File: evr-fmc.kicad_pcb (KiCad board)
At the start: 6 copper layers, 84 x 69 mm, 255 parts, among them J1 MMCX, J10 MMCX, J11 MMCX, J12 MMCX, J13 MMCX, J14 MMCX, J15 MMCX, J16 MMCX, J19 WP Jumper, J2 MMCX, J3 MMCX, J4 MMCX, J5 MMCX, J6 MMCX, J7 MMCX, J8 MMCX, J9 MMCX, P1 ASP-134488-01, Q1 FDN335N, Q2 FDN335N, Q3 FDN335N, T1 TCM2-43X+, T2 TCM2-43X+, T3 TCM2-43X+, T4 TCM2-43X+, U1 SN74LVC3G34DCT, U10 SN74LVC3G34DCT, U11 SN74LVC3G34DCT, U12 SN74LVC3G34DCT, U13 SN74LVC3G34DCT, U14 SN74LVC3G34DCT, U15 SN74LVC3G34DCT, U16 SN74LVC3G34DCT, U17 SN74LVC3G34DCT, U18 SI5394, U19 SI5394, U2 SN74LVC3G34DCT, U20 TLV75733PDBV, U21 TLV75718PDBV, U22 TPS562200, U23 74AVC4T245, U24 TLV75733PDBV, U25 74AVC4T245, U26 74LVC8T245, U27 74LVC8T245, U28 TLV75718PDBV, U3 SN74LVC3G34DCT, U4 SN74LVC3G34DCT, U5 SN74LVC3G34DCT, U6 SN74LVC3G34DCT, U7 SN74LVC3G34DCT, U8 SN74LVC3G34DCT, U9 AT24C64D, Y1 CX3225SB48000D0FPJC1, Y2 CX3225SB48000D0FPJC1

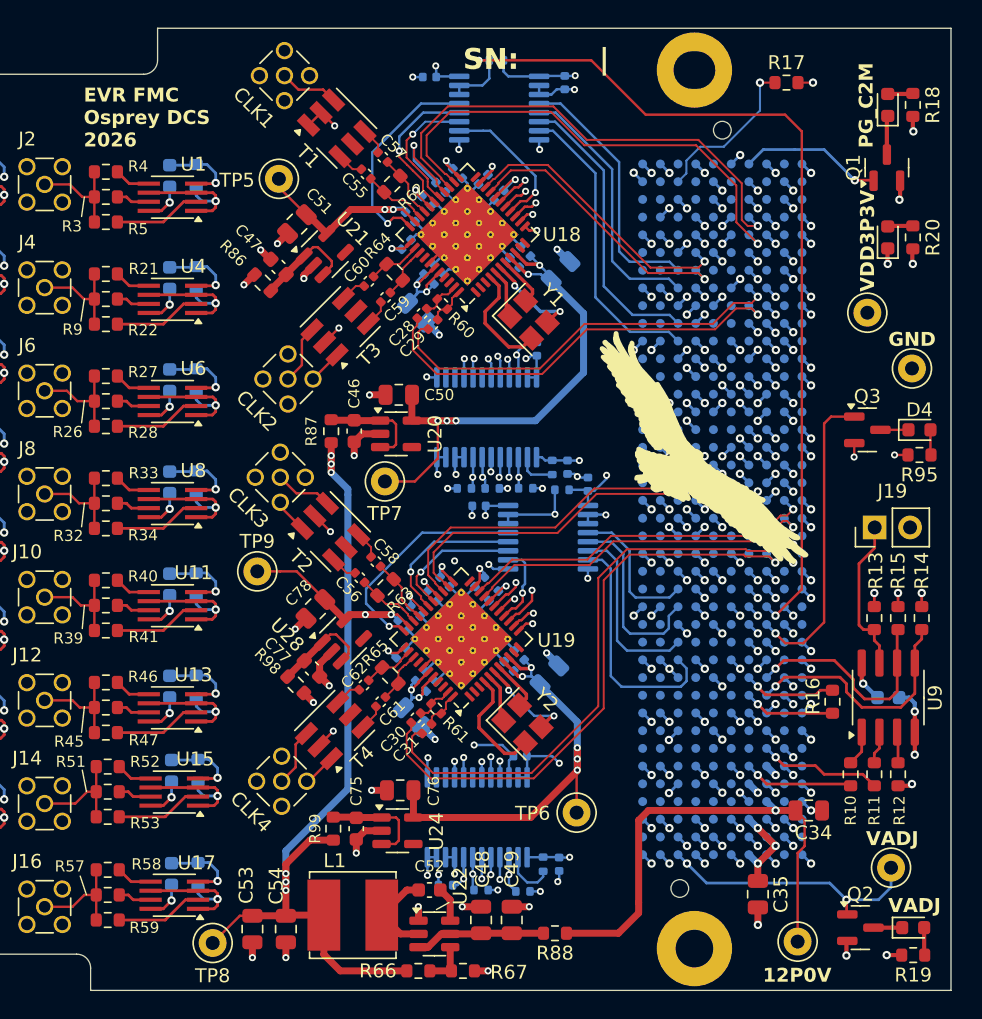
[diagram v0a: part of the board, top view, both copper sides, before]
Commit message: Final Draft - Ready for review
Updates:
- Changed area behind FMC connector to match the new Osprey FMC template
  - This includes a new 12V LED, more robust power input traces, arranged elements for readability.

Things to do:
Round diff traces before generating fabrication files
Change name of project to 'trigger output fmc'
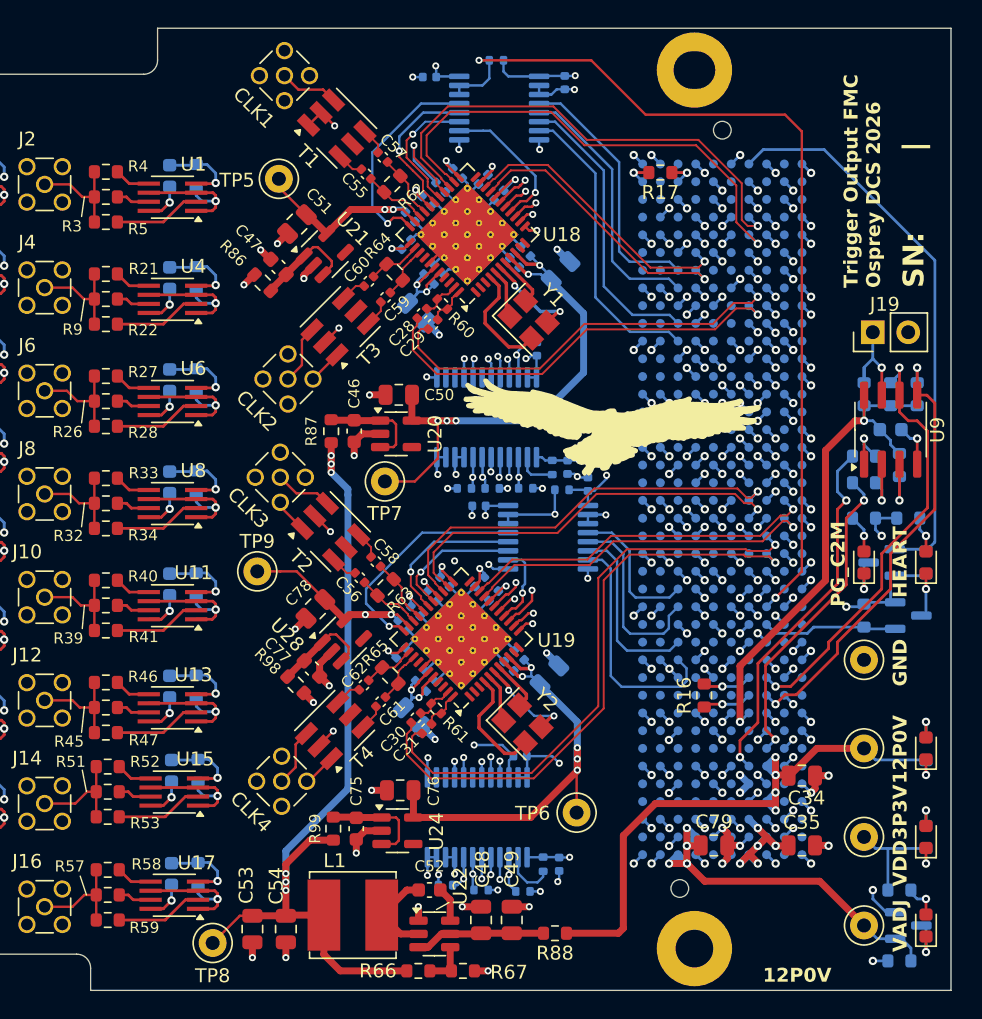
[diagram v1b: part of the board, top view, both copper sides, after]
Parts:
- added C79: 22uF, Capacitor_SMD:C_0805_2012Metric, F.Cu at (174.0, 129.6)
- added D5: Green, LED_SMD:LED_0603_1608Metric, F.Cu at (189.2, 122.6)
- added R100: 8.2k, Resistor_SMD:R_0603_1608Metric, B.Cu at (189.2, 122.7)
- added R101: 100k, Resistor_SMD:R_0603_1608Metric, B.Cu at (189.2, 109.3)
- added R102: 100k, Resistor_SMD:R_0603_1608Metric, B.Cu at (187.3, 137.9)
- added R103: 100k, Resistor_SMD:R_0603_1608Metric, B.Cu at (184.8, 113.1)
- D1, D2, D3, D4: value LED_Green -> Green
- Q1, Q2, Q3, R10, R11, R12, R13, R14, R15, R18, R19, R20, R95: moved to B.Cu
- TP5, TP9: value 1P8V -> Keystone5000
- TP6, TP7: value 3P3V -> Keystone5000
- TP8: value 4P3V -> Keystone5000
- moved D3 43.1 mm to (189.2, 129.0)
- moved R20 43.0 mm to (189.2, 129.0)
- moved TP3 37.6 mm to (184.8, 129.0)
- moved D1 32.9 mm to (184.8, 109.3)
- moved R18 29.8 mm to (184.8, 106.1), turned to 0 degrees
- moved Q1 28.3 mm to (186.0, 109.3), turned to 180 degrees
- moved R10 22.8 mm to (184.8, 101.7), turned to 0 degrees
- moved R12 22.2 mm to (187.3, 102.3), turned to -90 degrees
- moved TP1 21.2 mm to (184.8, 116.3)
- moved R11 20.9 mm to (184.8, 103.6), turned to 0 degrees
- moved C33 19.2 mm to (186.7, 99.8)
- moved U9 19.2 mm to (186.7, 99.8)
- moved R13 16.1 mm to (184.8, 97.2), turned to 90 degrees
- moved R15 16.1 mm to (186.7, 97.2), turned to 90 degrees
- moved R14 16.1 mm to (188.6, 97.2), turned to 90 degrees
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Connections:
- net /FMC/Heartbeat_LED renamed Heartbeat_LED
- net P1_3P3VAUX renamed 3P3VAUX
- net P1_PG_C2M renamed PG_C2M
- net P1_PRSNT renamed PRSNT
- net P1_TDI renamed TDI
- net P1_TDO renamed TDO
- net P1_VADJ renamed VADJ
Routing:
- net PG_C2M: track 10.3 -> 40.5 mm, vias 1 -> 0
- net /FMC/EEPROM_GA1: track 7.88 -> 26.4 mm, vias 1 -> 2
- net /FMC/EEPROM_SCL: track 16.1 -> 31.5 mm, vias 1 -> 2
- net /FMC/EEPROM_SDA: track 17.6 -> 32.3 mm, vias 1 -> 2
- net /FMC/EEPROM_GA0: track 8.83 -> 22.9 mm, vias 1 -> 2
- net GND: track 402.1 -> 415.6 mm
- net Heartbeat_LED: track 21.9 -> 9.80 mm, vias 1 -> 0
- net VDD3P3V: track 83.2 -> 94.4 mm
- net PRSNT: track 11.6 -> 2.00 mm
- net VADJ: track 75.6 -> 83.2 mm, vias 20 -> 21
- net Net-(J19-Pin_1): track 11.3 -> 7.85 mm, vias 0 -> 1
- net +12V_FMC: track 39.1 -> 42.4 mm, vias 2 -> 4
- net TDI: track 6.67 -> 3.54 mm
- net TDO: track 6.53 -> 3.55 mm
- net Net-(D5-A): track 0.00 -> 2.20 mm, vias 0 -> 1
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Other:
- board text added: "HEART"
- board text added: "Trigger Output FMC Osprey DCS 2026"
- board text removed: "EVR FMC Osprey DCS 2026"

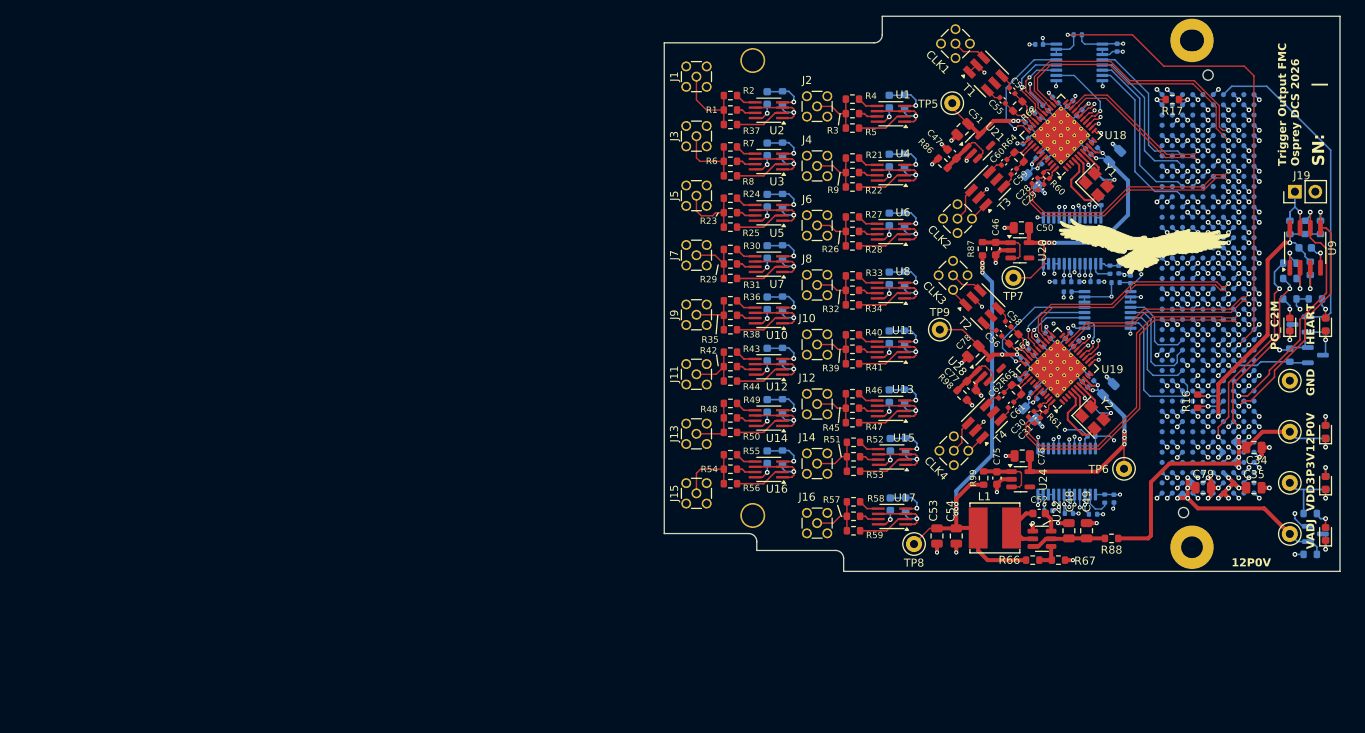
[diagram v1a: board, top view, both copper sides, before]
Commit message: Changed Trigger Outputs Topology
- Changed to a comp to digital TX design
- Added power section to support this change
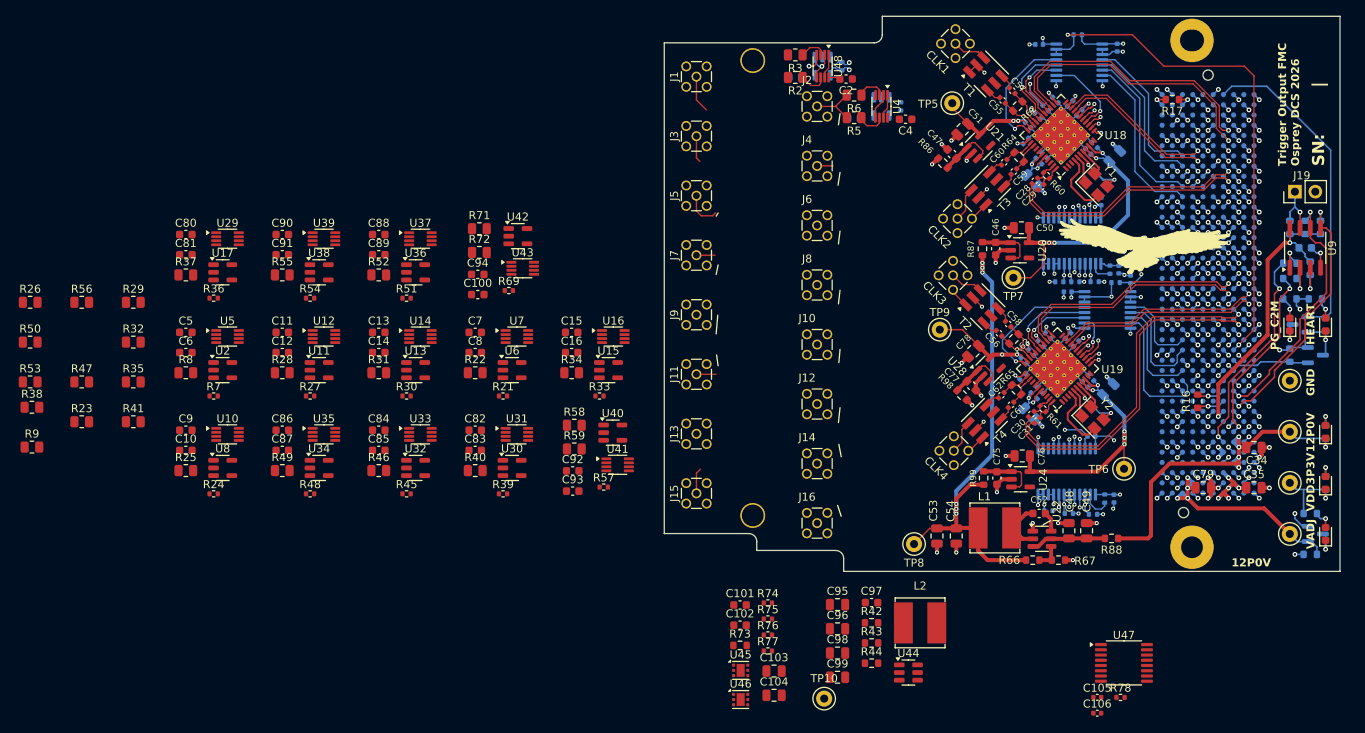
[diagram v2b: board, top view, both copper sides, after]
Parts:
- removed R79, R80, R81, R82, R83, R84, R85: 11.5k, Resistor_SMD:R_0603_1608Metric
- added C100: 100n, Capacitor_SMD:C_0603_1608Metric, F.Cu at (83.8, 105.6)
- added C101: 1uF, Capacitor_SMD:C_0603_1608Metric, F.Cu at (116.4, 144.2)
- added C102: 1uF, Capacitor_SMD:C_0603_1608Metric, F.Cu at (116.4, 146.7)
- added C103: 10uF, Capacitor_SMD:C_0805_2012Metric, F.Cu at (120.7, 152.4)
- added C104: 10uF, Capacitor_SMD:C_0805_2012Metric, F.Cu at (120.7, 155.4)
- added C105: 100nF, Capacitor_SMD:C_0402_1005Metric, F.Cu at (160.8, 155.7)
- added C106: 100nF, Capacitor_SMD:C_0402_1005Metric, F.Cu at (160.8, 157.6)
- added C80: 100n, Capacitor_SMD:C_0603_1608Metric, F.Cu at (47.5, 98.1)
- added C81: 100n, Capacitor_SMD:C_0603_1608Metric, F.Cu at (47.5, 100.6)
- added C82: 100n, Capacitor_SMD:C_0603_1608Metric, F.Cu at (83.5, 122.5)
- added C83: 100n, Capacitor_SMD:C_0603_1608Metric, F.Cu at (83.5, 125.0)
- added C84: 100n, Capacitor_SMD:C_0603_1608Metric, F.Cu at (71.5, 122.5)
- added C85: 100n, Capacitor_SMD:C_0603_1608Metric, F.Cu at (71.5, 125.0)
- added C86: 100n, Capacitor_SMD:C_0603_1608Metric, F.Cu at (59.5, 122.5)
- added C87: 100n, Capacitor_SMD:C_0603_1608Metric, F.Cu at (59.5, 125.0)
- added C88: 100n, Capacitor_SMD:C_0603_1608Metric, F.Cu at (71.5, 98.1)
- added C89: 100n, Capacitor_SMD:C_0603_1608Metric, F.Cu at (71.5, 100.6)
- added C90: 100n, Capacitor_SMD:C_0603_1608Metric, F.Cu at (59.5, 98.1)
- added C91: 100n, Capacitor_SMD:C_0603_1608Metric, F.Cu at (59.5, 100.6)
- added C92: 100n, Capacitor_SMD:C_0603_1608Metric, F.Cu at (95.6, 127.5)
- added C93: 100n, Capacitor_SMD:C_0603_1608Metric, F.Cu at (95.6, 130.0)
- added C94: 100n, Capacitor_SMD:C_0603_1608Metric, F.Cu at (83.8, 103.1)
- added C95: 10uF, Capacitor_SMD:C_0805_2012Metric, F.Cu at (128.5, 144.1)
- added C96: 10uF, Capacitor_SMD:C_0805_2012Metric, F.Cu at (128.5, 147.1)
- added C97: 100nF, Capacitor_SMD:C_0603_1608Metric, F.Cu at (132.8, 143.9)
- added C98: 22uF, Capacitor_SMD:C_0805_2012Metric, F.Cu at (128.5, 150.2)
- added C99: 22uF, Capacitor_SMD:C_0805_2012Metric, F.Cu at (128.5, 153.2)
- added L2: SRN6045TA-4R7M, Inductor_SMD:L_Bourns_SRN6045TA, F.Cu at (138.8, 146.4)
- added TP10: Keystone5000, TestPoint:TestPoint_Keystone_5000-5004_Miniature, F.Cu at (126.9, 155.8)
- added U29: SN74LVC2G126, Package_SO:VSSOP-8_2.3x2mm_P0.5mm, F.Cu at (52.7, 98.7)
- added U30: TLV3601, Package_TO_SOT_SMD:SOT-23-5, F.Cu at (88.1, 127.1)
- added U31: SN74LVC2G126, Package_SO:VSSOP-8_2.3x2mm_P0.5mm, F.Cu at (88.7, 123.0)
- added U32: TLV3601, Package_TO_SOT_SMD:SOT-23-5, F.Cu at (76.1, 127.1)
- added U33: SN74LVC2G126, Package_SO:VSSOP-8_2.3x2mm_P0.5mm, F.Cu at (76.7, 123.0)
- added U34: TLV3601, Package_TO_SOT_SMD:SOT-23-5, F.Cu at (64.1, 127.1)
- added U35: SN74LVC2G126, Package_SO:VSSOP-8_2.3x2mm_P0.5mm, F.Cu at (64.7, 123.0)
- added U36: TLV3601, Package_TO_SOT_SMD:SOT-23-5, F.Cu at (76.1, 102.8)
- added U37: SN74LVC2G126, Package_SO:VSSOP-8_2.3x2mm_P0.5mm, F.Cu at (76.7, 98.7)
- added U38: TLV3601, Package_TO_SOT_SMD:SOT-23-5, F.Cu at (64.1, 102.8)
- added U39: SN74LVC2G126, Package_SO:VSSOP-8_2.3x2mm_P0.5mm, F.Cu at (64.7, 98.7)
- added U40: TLV3601, Package_TO_SOT_SMD:SOT-23-5, F.Cu at (100.6, 122.8)
- added U41: SN74LVC2G126, Package_SO:VSSOP-8_2.3x2mm_P0.5mm, F.Cu at (101.2, 126.8)
- added U42: TLV3601, Package_TO_SOT_SMD:SOT-23-5, F.Cu at (88.8, 98.3)
- added U43: SN74LVC2G126, Package_SO:VSSOP-8_2.3x2mm_P0.5mm, F.Cu at (89.4, 102.3)
- added U44: TPS562200, Package_TO_SOT_SMD:SOT-23-6, F.Cu at (137.3, 152.6)
- added U45: TLV75901PDRV, Package_SON:WSON-6-1EP_2x2mm_P0.65mm_EP1x1.6mm, F.Cu at (116.5, 152.3)
- added U46: TLV75901PDRV, Package_SON:WSON-6-1EP_2x2mm_P0.65mm_EP1x1.6mm, F.Cu at (116.5, 155.9)
- added U47: 74AVC4T245, Package_SO:TSSOP-16_4.4x5mm_P0.65mm, F.Cu at (164.1, 151.4)
- added U48: SN74LVC2G126, Package_SO:VSSOP-8_2.3x2mm_P0.5mm, F.Cu at (126.7, 77.2)
- C10, C11, C12, C13, C14, C15, C16, C2, C4, C5, C6, C7, C8, C9: moved to F.Cu
- R1, R4: value 10 -> 100R; footprint Resistor_SMD:R_0603_1608Metric -> Resistor_SMD:R_0402_1005Metric; moved to B.Cu
- R2, R22, R23, R25, R26, R28, R29, R3, R31, R32, R34, R35, R37, R38, R40, R41, R46, R47, R49, R5, R50, R52, R53, R55, R56, R58, R59, R6, R8, R9: value 10 -> 88.7R; footprint Resistor_SMD:R_0603_1608Metric -> Resistor_SMD:R_0805_2012Metric
- R21, R24, R27, R30, R33, R36, R39, R45, R48, R51, R54, R57, R7: value 10 -> 100R; footprint Resistor_SMD:R_0603_1608Metric -> Resistor_SMD:R_0402_1005Metric
- R42: value 10 -> 0R
- R43: value 10 -> 62k
- R44: value 10 -> 10k
- R69: value 11.5k -> 100R; footprint Resistor_SMD:R_0603_1608Metric -> Resistor_SMD:R_0402_1005Metric; moved to F.Cu
- R71, R72: value 11.5k -> 88.7R; footprint Resistor_SMD:R_0603_1608Metric -> Resistor_SMD:R_0805_2012Metric; moved to F.Cu
- R73: value 11.5k -> 0R; moved to F.Cu
- R74, R77: value 11.5k -> 10.7k; footprint Resistor_SMD:R_0603_1608Metric -> Resistor_SMD:R_0402_1005Metric; moved to F.Cu
- R75, R76: value 11.5k -> 86.6k; footprint Resistor_SMD:R_0603_1608Metric -> Resistor_SMD:R_0402_1005Metric; moved to F.Cu
- R78: value 11.5k -> 4.75k; footprint Resistor_SMD:R_0603_1608Metric -> Resistor_SMD:R_0402_1005Metric; moved to F.Cu
- U1, U3: value SN74LVC3G34DCT -> TLV3601; footprint Package_SO:SSOP-8_2.95x2.8mm_P0.65mm -> Package_TO_SOT_SMD:SOT-23-5; moved to B.Cu
- U10, U12, U14, U16, U4, U5, U7: value SN74LVC3G34DCT -> SN74LVC2G126; footprint Package_SO:SSOP-8_2.95x2.8mm_P0.65mm -> Package_SO:VSSOP-8_2.3x2mm_P0.5mm
- U11, U13, U15, U17, U2, U6, U8: value SN74LVC3G34DCT -> TLV3601; footprint Package_SO:SSOP-8_2.95x2.8mm_P0.65mm -> Package_TO_SOT_SMD:SOT-23-5
- moved R9 107.6 mm to (28.4, 124.5), turned to 0 degrees
- moved R53 102.9 mm to (28.2, 116.5), turned to 0 degrees
- moved R26 102.6 mm to (28.2, 106.5), turned to 0 degrees
- moved R47 95.9 mm to (34.6, 116.5), turned to 0 degrees
- moved R41 89.7 mm to (41.0, 121.4), turned to 0 degrees
- moved R32 89.6 mm to (41.0, 111.5), turned to 0 degrees
- moved C6 89.0 mm to (47.5, 112.8), turned to 0 degrees
- moved C10 88.6 mm to (47.5, 125.0), turned to 0 degrees
- moved U17 88.6 mm to (52.1, 102.8), turned to 0 degrees
- moved R50 87.8 mm to (28.2, 111.5), turned to 0 degrees
- moved R38 87.4 mm to (28.4, 119.6), turned to 0 degrees
- moved U8 85.9 mm to (52.1, 127.1), turned to 0 degrees
- moved R23 84.7 mm to (34.6, 121.4), turned to 0 degrees
- moved R56 83.7 mm to (34.6, 106.5), turned to 0 degrees
- moved C12 75.6 mm to (59.5, 112.8), turned to 0 degrees
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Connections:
- C1 pad 2: VDD3P3V -> /Digital IO/VCC_A
- C10 pad 2: VDD3P3V -> /Digital IO/VCC_A
- C11 pad 2: VDD3P3V -> /Digital IO/VCC_A
- C12 pad 2: VDD3P3V -> /Digital IO/VCC_A
- C13 pad 2: VDD3P3V -> /Digital IO/VCC_A
- C14 pad 2: VDD3P3V -> /Digital IO/VCC_A
- C15 pad 2: VDD3P3V -> /Digital IO/VCC_A
- C16 pad 2: VDD3P3V -> /Digital IO/VCC_A
- C2 pad 2: VDD3P3V -> /Digital IO/VCC_A
- C3 pad 2: VDD3P3V -> /Digital IO/VCC_A
- C4 pad 2: VDD3P3V -> /Digital IO/VCC_A
- C5 pad 2: VDD3P3V -> /Digital IO/VCC_A
- C6 pad 2: VDD3P3V -> /Digital IO/VCC_A
- C7 pad 2: VDD3P3V -> /Digital IO/VCC_A
- C8 pad 2: VDD3P3V -> /Digital IO/VCC_A
- C9 pad 2: VDD3P3V -> /Digital IO/VCC_A
- P1 pad C14: /Digital IO/D_Output6 -> /Digital IO/D_Output3.P
- P1 pad C15: /Digital IO/D_Output7 -> /Digital IO/D_Output3.N
- P1 pad C18: /Digital IO/D_Output14 -> /Digital IO/D_Output7.P
- P1 pad C19: /Digital IO/D_Output15 -> /Digital IO/D_Output7.N
- P1 pad D14: /Digital IO/D_Output2 -> /Digital IO/D_Output2.P
- P1 pad D15: /Digital IO/D_Output3 -> /Digital IO/D_Output2.N
- P1 pad D17: /Digital IO/D_Output10 -> /Digital IO/D_Output6.P
- P1 pad D18: /Digital IO/D_Output11 -> /Digital IO/D_Output6.N
- P1 pad G12: /Digital IO/D_Output0 -> /Digital IO/D_Output0.P
- P1 pad G13: /Digital IO/D_Output1 -> /Digital IO/D_Output0.N
- P1 pad G15: /Digital IO/D_Output4 -> /Digital IO/D_Output4.P
- P1 pad G16: /Digital IO/D_Output5 -> /Digital IO/D_Output4.N
- P1 pad G18: /Digital IO/D_Output8 -> /Digital IO/D_Output8.P
- P1 pad G19: /Digital IO/D_Output9 -> /Digital IO/D_Output8.N
- P1 pad G21: /Digital IO/D_Output12 -> /Digital IO/D_Output10.P
- P1 pad G22: /Digital IO/D_Output13 -> /Digital IO/D_Output10.N
- P1 pad G27: unconnected-(P1-PadG27) -> /Digital IO/D_Output11.P
- P1 pad G28: unconnected-(P1-PadG28) -> /Digital IO/D_Output11.N
- P1 pad G30: unconnected-(P1-PadG30) -> /Digital IO/D_Output12.P
- P1 pad G31: unconnected-(P1-PadG31) -> /Digital IO/D_Output12.N
- P1 pad G33: unconnected-(P1-PadG33) -> /Digital IO/D_Output14.P
- P1 pad G34: unconnected-(P1-PadG34) -> /Digital IO/D_Output14.N
- P1 pad G36: unconnected-(P1-PadG36) -> /Digital IO/OE
- P1 pad H13: unconnected-(P1-PadH13) -> /Digital IO/D_Output1.P
- P1 pad H14: unconnected-(P1-PadH14) -> /Digital IO/D_Output1.N
- P1 pad H16: unconnected-(P1-PadH16) -> /Digital IO/D_Output5.P
- P1 pad H17: unconnected-(P1-PadH17) -> /Digital IO/D_Output5.N
- P1 pad H19: unconnected-(P1-PadH19) -> /Digital IO/D_Output9.P
- P1 pad H20: unconnected-(P1-PadH20) -> /Digital IO/D_Output9.N
- P1 pad H31: unconnected-(P1-PadH31) -> /Digital IO/D_Output13.P
- P1 pad H32: unconnected-(P1-PadH32) -> /Digital IO/D_Output13.N
- P1 pad H34: unconnected-(P1-PadH34) -> /Digital IO/D_Output15.P
- P1 pad H35: unconnected-(P1-PadH35) -> /Digital IO/D_Output15.N
- R1 pad 1: Net-(U2-1Y) -> /Digital IO/D_Output0.P
- R1 pad 2: /Digital IO/out_buffer0/Out -> /Digital IO/D_Output0.N
- R2 pad 1: Net-(U2-2Y) -> Net-(U48-1Y)
- R21 pad 1: Net-(U4-2Y) -> /Digital IO/D_Output3.P
- R21 pad 2: /Digital IO/out_buffer3/Out -> /Digital IO/D_Output3.N
- R22 pad 1: Net-(U4-3Y) -> Net-(U7-1Y)
- R23 pad 1: Net-(U5-1Y) -> Net-(U7-2Y)
- R23 pad 2: /Digital IO/out_buffer4/Out -> /Digital IO/out_buffer3/Out
- R24 pad 1: Net-(U5-2Y) -> /Digital IO/D_Output4.P
- R24 pad 2: /Digital IO/out_buffer4/Out -> /Digital IO/D_Output4.N
- R25 pad 1: Net-(U5-3Y) -> Net-(U10-1Y)
- R26 pad 1: Net-(U6-1Y) -> Net-(U10-2Y)
- R26 pad 2: /Digital IO/out_buffer5/Out -> /Digital IO/out_buffer4/Out
- R27 pad 1: Net-(U6-2Y) -> /Digital IO/D_Output5.P
- R27 pad 2: /Digital IO/out_buffer5/Out -> /Digital IO/D_Output5.N
- R28 pad 1: Net-(U6-3Y) -> Net-(U12-1Y)
- R29 pad 1: Net-(U7-1Y) -> Net-(U12-2Y)
- R29 pad 2: /Digital IO/out_buffer6/Out -> /Digital IO/out_buffer5/Out
- R3 pad 1: Net-(U1-1Y) -> Net-(U48-2Y)
- R3 pad 2: /Digital IO/out_buffer1/Out -> /Digital IO/out_buffer0/Out
- R30 pad 1: Net-(U7-2Y) -> /Digital IO/D_Output6.P
- R30 pad 2: /Digital IO/out_buffer6/Out -> /Digital IO/D_Output6.N
- R31 pad 1: Net-(U7-3Y) -> Net-(U14-1Y)
- R32 pad 1: Net-(U8-1Y) -> Net-(U14-2Y)
- R32 pad 2: /Digital IO/out_buffer7/Out -> /Digital IO/out_buffer6/Out
- R33 pad 1: Net-(U8-2Y) -> /Digital IO/D_Output7.P
- R33 pad 2: /Digital IO/out_buffer7/Out -> /Digital IO/D_Output7.N
- R34 pad 1: Net-(U8-3Y) -> Net-(U16-1Y)
- R35 pad 1: Net-(U10-1Y) -> Net-(U16-2Y)
- R35 pad 2: /Digital IO/out_buffer8/Out -> /Digital IO/out_buffer7/Out
- R36 pad 1: Net-(U10-2Y) -> /Digital IO/D_Output8.P
- R36 pad 2: /Digital IO/out_buffer8/Out -> /Digital IO/D_Output8.N
- R37 pad 1: Net-(U2-3Y) -> Net-(U29-1Y)
- R37 pad 2: /Digital IO/out_buffer0/Out -> /Digital IO/out_buffer8/Out
- R38 pad 1: Net-(U10-3Y) -> Net-(U29-2Y)
- R39 pad 1: Net-(U11-1Y) -> /Digital IO/D_Output9.P
- R39 pad 2: /Digital IO/out_buffer9/Out -> /Digital IO/D_Output9.N
- R4 pad 1: Net-(U1-2Y) -> /Digital IO/D_Output1.P
- R4 pad 2: /Digital IO/out_buffer1/Out -> /Digital IO/D_Output1.N
- R40 pad 1: Net-(U11-2Y) -> Net-(U31-1Y)
- R41 pad 1: Net-(U11-3Y) -> Net-(U31-2Y)
- R42 pad 1: Net-(U12-1Y) -> +12V_FMC
- R42 pad 2: /Digital IO/out_buffer10/Out -> Net-(U44-EN)
- R43 pad 1: Net-(U12-2Y) -> /Digital IO/Switched_5P5V
- R43 pad 2: /Digital IO/out_buffer10/Out -> Net-(U44-VFB)
- R44 pad 1: Net-(U12-3Y) -> Net-(U44-VFB)
- R44 pad 2: /Digital IO/out_buffer10/Out -> GND
- R45 pad 1: Net-(U13-1Y) -> /Digital IO/D_Output10.P
- R45 pad 2: /Digital IO/out_buffer11/Out -> /Digital IO/D_Output10.N
- R46 pad 1: Net-(U13-2Y) -> Net-(U33-1Y)
- R46 pad 2: /Digital IO/out_buffer11/Out -> /Digital IO/out_buffer10/Out
- R47 pad 1: Net-(U13-3Y) -> Net-(U33-2Y)
- R47 pad 2: /Digital IO/out_buffer11/Out -> /Digital IO/out_buffer10/Out
- R48 pad 1: Net-(U14-1Y) -> /Digital IO/D_Output11.P
- R48 pad 2: /Digital IO/out_buffer12/Out -> /Digital IO/D_Output11.N
- R49 pad 1: Net-(U14-2Y) -> Net-(U35-1Y)
- R49 pad 2: /Digital IO/out_buffer12/Out -> /Digital IO/out_buffer11/Out
- R5 pad 1: Net-(U1-3Y) -> Net-(U4-1Y)
- R50 pad 1: Net-(U14-3Y) -> Net-(U35-2Y)
- R50 pad 2: /Digital IO/out_buffer12/Out -> /Digital IO/out_buffer11/Out
- R51 pad 1: Net-(U15-1Y) -> /Digital IO/D_Output12.P
- R51 pad 2: /Digital IO/out_buffer13/Out -> /Digital IO/D_Output12.N
- R52 pad 1: Net-(U15-2Y) -> Net-(U37-1Y)
- R52 pad 2: /Digital IO/out_buffer13/Out -> /Digital IO/out_buffer12/Out
- R53 pad 1: Net-(U15-3Y) -> Net-(U37-2Y)
- R53 pad 2: /Digital IO/out_buffer13/Out -> /Digital IO/out_buffer12/Out
- R54 pad 1: Net-(U16-1Y) -> /Digital IO/D_Output13.P
- R54 pad 2: /Digital IO/out_buffer14/Out -> /Digital IO/D_Output13.N
- R55 pad 1: Net-(U16-2Y) -> Net-(U39-1Y)
- R55 pad 2: /Digital IO/out_buffer14/Out -> /Digital IO/out_buffer13/Out
- R56 pad 1: Net-(U16-3Y) -> Net-(U39-2Y)
- R56 pad 2: /Digital IO/out_buffer14/Out -> /Digital IO/out_buffer13/Out
- R57 pad 1: Net-(U17-1Y) -> /Digital IO/D_Output14.P
- R57 pad 2: /Digital IO/out_buffer15/Out -> /Digital IO/D_Output14.N
- R58 pad 1: Net-(U17-2Y) -> Net-(U41-1Y)
- R58 pad 2: /Digital IO/out_buffer15/Out -> /Digital IO/out_buffer14/Out
- R59 pad 1: Net-(U17-3Y) -> Net-(U41-2Y)
- R59 pad 2: /Digital IO/out_buffer15/Out -> /Digital IO/out_buffer14/Out
- R6 pad 1: Net-(U3-1Y) -> Net-(U4-2Y)
- R6 pad 2: /Digital IO/out_buffer2/Out -> /Digital IO/out_buffer1/Out
- R69 pad 1: /Digital IO/D_Output0 -> /Digital IO/D_Output15.P
- R69 pad 2: GND -> /Digital IO/D_Output15.N
- R7 pad 1: Net-(U3-2Y) -> /Digital IO/D_Output2.P
- R7 pad 2: /Digital IO/out_buffer2/Out -> /Digital IO/D_Output2.N
- R71 pad 1: /Digital IO/D_Output1 -> Net-(U43-1Y)
- R71 pad 2: GND -> /Digital IO/out_buffer15/Out
- R72 pad 1: /Digital IO/D_Output2 -> Net-(U43-2Y)
- R72 pad 2: GND -> /Digital IO/out_buffer15/Out
- R73 pad 1: /Digital IO/D_Output3 -> /Digital IO/Switched_5P5V
- R73 pad 2: GND -> Net-(U45-EN)
- R74 pad 1: /Digital IO/D_Output4 -> GND
- R74 pad 2: GND -> Net-(U45-FB)
- R75 pad 1: /Digital IO/D_Output5 -> Net-(U45-FB)
- R75 pad 2: GND -> /Digital IO/VCC_A
- R76 pad 1: /Digital IO/D_Output6 -> Net-(U46-FB)
- R76 pad 2: GND -> /Digital IO/VCC_B
- R77 pad 1: /Digital IO/D_Output7 -> GND
- R77 pad 2: GND -> Net-(U46-FB)
- R78 pad 1: /Digital IO/D_Output8 -> Net-(U47-1DIR)
- R78 pad 2: GND -> VADJ
- R8 pad 1: Net-(U3-3Y) -> Net-(U5-1Y)
- R9 pad 1: Net-(U4-1Y) -> Net-(U5-2Y)
- R9 pad 2: /Digital IO/out_buffer3/Out -> /Digital IO/out_buffer2/Out
- U1 pad 1: /Digital IO/D_Output1 -> Net-(U48-1A)
- U1 pad 2: Net-(U1-3Y) -> GND
- U1 pad 3: /Digital IO/D_Output1 -> /Digital IO/D_Output0.P
- U1 pad 4: GND -> /Digital IO/D_Output0.N
- U1 pad 5: Net-(U1-2Y) -> /Digital IO/VCC_A
- U10 pad 1: /Digital IO/D_Output8 -> /Digital IO/OE
- U10 pad 2: Net-(U10-3Y) -> Net-(U10-1A)
- U10 pad 3: /Digital IO/D_Output8 -> Net-(U10-2Y)
- U10 pad 5: Net-(U10-2Y) -> Net-(U10-1A)
- U10 pad 6: /Digital IO/D_Output8 -> Net-(U10-1Y)
- U10 pad 7: Net-(U10-1Y) -> /Digital IO/OE
- U10 pad 8: VDD3P3V -> /Digital IO/VCC_A
- U11 pad 1: /Digital IO/D_Output9 -> Net-(U12-1A)
- U11 pad 2: Net-(U11-3Y) -> GND
- U11 pad 3: /Digital IO/D_Output9 -> /Digital IO/D_Output5.P
- U11 pad 4: GND -> /Digital IO/D_Output5.N
- U11 pad 5: Net-(U11-2Y) -> /Digital IO/VCC_A
- U12 pad 1: /Digital IO/D_Output10 -> /Digital IO/OE
- U12 pad 2: Net-(U12-3Y) -> Net-(U12-1A)
- U12 pad 3: /Digital IO/D_Output10 -> Net-(U12-2Y)
- U12 pad 5: Net-(U12-2Y) -> Net-(U12-1A)
- U12 pad 6: /Digital IO/D_Output10 -> Net-(U12-1Y)
- U12 pad 7: Net-(U12-1Y) -> /Digital IO/OE
- U12 pad 8: VDD3P3V -> /Digital IO/VCC_A
- U13 pad 1: /Digital IO/D_Output11 -> Net-(U14-1A)
- U13 pad 2: Net-(U13-3Y) -> GND
- U13 pad 3: /Digital IO/D_Output11 -> /Digital IO/D_Output6.P
- U13 pad 4: GND -> /Digital IO/D_Output6.N
- U13 pad 5: Net-(U13-2Y) -> /Digital IO/VCC_A
- U14 pad 1: /Digital IO/D_Output12 -> /Digital IO/OE
- U14 pad 2: Net-(U14-3Y) -> Net-(U14-1A)
- U14 pad 3: /Digital IO/D_Output12 -> Net-(U14-2Y)
- U14 pad 5: Net-(U14-2Y) -> Net-(U14-1A)
- U14 pad 6: /Digital IO/D_Output12 -> Net-(U14-1Y)
- U14 pad 7: Net-(U14-1Y) -> /Digital IO/OE
- U14 pad 8: VDD3P3V -> /Digital IO/VCC_A
- U15 pad 1: /Digital IO/D_Output13 -> Net-(U16-1A)
- U15 pad 2: Net-(U15-3Y) -> GND
- U15 pad 3: /Digital IO/D_Output13 -> /Digital IO/D_Output7.P
- U15 pad 4: GND -> /Digital IO/D_Output7.N
- U15 pad 5: Net-(U15-2Y) -> /Digital IO/VCC_A
- U16 pad 1: /Digital IO/D_Output14 -> /Digital IO/OE
- U16 pad 2: Net-(U16-3Y) -> Net-(U16-1A)
- U16 pad 3: /Digital IO/D_Output14 -> Net-(U16-2Y)
- U16 pad 5: Net-(U16-2Y) -> Net-(U16-1A)
- U16 pad 6: /Digital IO/D_Output14 -> Net-(U16-1Y)
- U16 pad 7: Net-(U16-1Y) -> /Digital IO/OE
- U16 pad 8: VDD3P3V -> /Digital IO/VCC_A
- U17 pad 1: /Digital IO/D_Output15 -> Net-(U29-1A)
- U17 pad 2: Net-(U17-3Y) -> GND
- U17 pad 3: /Digital IO/D_Output15 -> /Digital IO/D_Output8.P
- U17 pad 4: GND -> /Digital IO/D_Output8.N
- U17 pad 5: Net-(U17-2Y) -> /Digital IO/VCC_B
- U2 pad 1: /Digital IO/D_Output0 -> Net-(U5-1A)
- U2 pad 2: Net-(U2-3Y) -> GND
- U2 pad 3: /Digital IO/D_Output0 -> /Digital IO/D_Output2.P
- U2 pad 4: GND -> /Digital IO/D_Output2.N
- U2 pad 5: Net-(U2-2Y) -> /Digital IO/VCC_A
- U26 pad 10: GND -> unconnected-(U26-A8-Pad10)
- U26 pad 6: GND -> unconnected-(U26-A4-Pad6)
- U26 pad 9: GND -> unconnected-(U26-A7-Pad9)
- U27 pad 10: GND -> unconnected-(U27-A8-Pad10)
- U27 pad 6: GND -> unconnected-(U27-A4-Pad6)
- U27 pad 9: GND -> unconnected-(U27-A7-Pad9)
- U3 pad 1: /Digital IO/D_Output2 -> Net-(U4-1A)
- U3 pad 2: Net-(U3-3Y) -> GND
- U3 pad 3: /Digital IO/D_Output2 -> /Digital IO/D_Output1.P
- U3 pad 4: GND -> /Digital IO/D_Output1.N
- U3 pad 5: Net-(U3-2Y) -> /Digital IO/VCC_A
- U4 pad 1: /Digital IO/D_Output3 -> /Digital IO/OE
- U4 pad 2: Net-(U4-3Y) -> Net-(U4-1A)
- U4 pad 3: /Digital IO/D_Output3 -> Net-(U4-2Y)
- U4 pad 5: Net-(U4-2Y) -> Net-(U4-1A)
- U4 pad 6: /Digital IO/D_Output3 -> Net-(U4-1Y)
- U4 pad 7: Net-(U4-1Y) -> /Digital IO/OE
- U4 pad 8: VDD3P3V -> /Digital IO/VCC_A
- U5 pad 1: /Digital IO/D_Output4 -> /Digital IO/OE
- U5 pad 2: Net-(U5-3Y) -> Net-(U5-1A)
- U5 pad 3: /Digital IO/D_Output4 -> Net-(U5-2Y)
- U5 pad 5: Net-(U5-2Y) -> Net-(U5-1A)
- U5 pad 6: /Digital IO/D_Output4 -> Net-(U5-1Y)
- U5 pad 7: Net-(U5-1Y) -> /Digital IO/OE
- U5 pad 8: VDD3P3V -> /Digital IO/VCC_A
- U6 pad 1: /Digital IO/D_Output5 -> Net-(U7-1A)
- U6 pad 2: Net-(U6-3Y) -> GND
- U6 pad 3: /Digital IO/D_Output5 -> /Digital IO/D_Output3.P
- U6 pad 4: GND -> /Digital IO/D_Output3.N
- U6 pad 5: Net-(U6-2Y) -> /Digital IO/VCC_A
- U7 pad 1: /Digital IO/D_Output6 -> /Digital IO/OE
- U7 pad 2: Net-(U7-3Y) -> Net-(U7-1A)
- U7 pad 3: /Digital IO/D_Output6 -> Net-(U7-2Y)
- U7 pad 5: Net-(U7-2Y) -> Net-(U7-1A)
- U7 pad 6: /Digital IO/D_Output6 -> Net-(U7-1Y)
- U7 pad 7: Net-(U7-1Y) -> /Digital IO/OE
- U7 pad 8: VDD3P3V -> /Digital IO/VCC_A
- U8 pad 1: /Digital IO/D_Output7 -> Net-(U10-1A)
- U8 pad 2: Net-(U8-3Y) -> GND
- U8 pad 3: /Digital IO/D_Output7 -> /Digital IO/D_Output4.P
- U8 pad 4: GND -> /Digital IO/D_Output4.N
- U8 pad 5: Net-(U8-2Y) -> /Digital IO/VCC_A
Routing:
- net GND: track 415.6 -> 324.9 mm, vias 228 -> 211
- net /Digital IO/D_Output14: track 83.5 -> 0.00 mm, vias 2 -> 0
- net /Digital IO/D_Output15: track 71.4 -> 0.00 mm, vias 2 -> 0
- net /Digital IO/D_Output10: track 70.5 -> 0.00 mm, vias 2 -> 0
- net /Digital IO/D_Output0: track 70.5 -> 0.00 mm, vias 2 -> 0
- net /Digital IO/D_Output2: track 69.5 -> 0.00 mm, vias 2 -> 0
- net /Digital IO/D_Output12: track 69.2 -> 0.00 mm, vias 2 -> 0
- net /Digital IO/D_Output6: track 66.1 -> 0.00 mm, vias 2 -> 0
- net /Digital IO/D_Output8: track 63.8 -> 0.00 mm, vias 2 -> 0
- net /Digital IO/D_Output4: track 63.0 -> 0.00 mm, vias 2 -> 0
- net /Digital IO/D_Output0.N: track 0.00 -> 59.8 mm, vias 0 -> 2
- net /Digital IO/D_Output0.P: track 0.00 -> 59.4 mm, vias 0 -> 2
- net /Digital IO/D_Output11: track 59.0 -> 0.00 mm, vias 2 -> 0
- net /Digital IO/D_Output13: track 56.1 -> 0.00 mm, vias 2 -> 0
- net /Digital IO/D_Output7: track 52.6 -> 0.00 mm, vias 2 -> 0
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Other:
- copper layers 6 -> 8
- board text added: "0"
- board text added: "0 mm"
- board text added: "0.01 mm"
- board text added: "0.02"
- board text added: "0.035 mm"
- board text added: "0.1525 mm"
- board text added: "0.23 mm"
- board text added: "1"
- board text added: "3.3"
- board text added: "4.3"
- board text added: "B.Cu"
- board text added: "B.Mask"
- board text added: "B.Paste"
- board text added: "B.Silkscreen"
- board text added: "Bottom Silk Screen"
- board text added: "Bottom Solder Mask"
- board text added: "Bottom Solder Paste"
- board text added: "Color"
- board text added: "Dielectric 1"
- board text added: "Dielectric 2"
- board text added: "Dielectric 3"
- board text added: "Dielectric 4"
- board text added: "Dielectric 5"
- board text added: "Dielectric 6"
- board text added: "Dielectric 7"
- board text added: "Epsilon R"
- board text added: "F.Cu"
- board text added: "F.Mask"
- board text added: "F.Paste"
- board text added: "F.Silkscreen"
- board text added: "FR4"
- board text added: "FR4 - 2113x2"
- board text added: "Green"
- board text added: "In1.Cu"
- board text added: "In2.Cu"
- board text added: "In3.Cu"
- board text added: "In4.Cu"
- board text added: "In5.Cu"
- board text added: "In6.Cu"
- board text added: "Layer Name"
- board text added: "Loss Tangent"
- board text added: "Material"
- board text added: "Not specified"
- board text added: "Thickness (mm)"
- board text added: "Top Silk Screen"
- board text added: "Top Solder Mask"
- board text added: "Top Solder Paste"
- board text added: "Type"
- board text added: "White"
- board text added: "copper"
- board text added: "core"
- board text added: "prepreg"

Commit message: Updated Layout - roughly floor planed all parts on board
- All parts fit on the board but routing may still result in power sections moving
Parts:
- removed C105, C106: 100nF, Capacitor_SMD:C_0402_1005Metric
- removed R78: 4.75k, Resistor_SMD:R_0402_1005Metric
- removed U47: 74AVC4T245, Package_SO:TSSOP-16_4.4x5mm_P0.65mm
- C11, C13, C15, C5, C7, C80, C82, C84, C86, C88, C9, C90, C92, C94, R21, R24, R27, R30, R33, R36, R39, R45, R48, R51, R54, R57, R69, R7, U11, U13, U15, U17, U2, U30, U32, U34, U36, U38, U40, U42, U6, U8: moved to B.Cu
- moved R73 104.8 mm to (189.6, 74.2), turned to -90 degrees
- moved R50 102.4 mm to (130.4, 117.8), turned to 180 degrees
- moved R23 101.4 mm to (130.4, 88.2), turned to 180 degrees
- moved TP10 99.8 mm to (183.2, 73.4), turned to -90 degrees
- moved C99 98.6 mm to (186.5, 73.4), turned to 180 degrees
- moved R56 97.6 mm to (130.4, 125.2), turned to 180 degrees
- moved R9 95.7 mm to (115.4, 84.6), turned to 180 degrees
- moved C98 94.3 mm to (186.5, 75.8), turned to 180 degrees
- moved R35 90.4 mm to (130.4, 103.0), turned to 180 degrees
- moved R41 90.1 mm to (130.4, 110.4), turned to 180 degrees
- moved R29 90.1 mm to (130.4, 95.6), turned to 180 degrees
- moved R26 88.4 mm to (115.4, 92.0), turned to 180 degrees
- moved R38 88.0 mm to (115.4, 106.6), turned to 180 degrees
- moved R53 87.3 mm to (115.4, 120.4), turned to 180 degrees
- moved U44 82.1 mm to (186.0, 86.4), turned to -90 degrees
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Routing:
- net GND: track 324.9 -> 392.0 mm, vias 211 -> 242
- net /Digital IO/OE: track 6.01 -> 48.1 mm
- net /Digital IO/VCC_B: track 0.00 -> 26.1 mm
- net /Digital IO/VCC_A: track 1.47 -> 26.1 mm
- net /Jitter Cleaner1/VDDA: track 36.4 -> 20.2 mm
- net +12V_FMC: track 42.4 -> 28.2 mm
- net /Jitter Cleaner0/Switched_4P3V: track 61.5 -> 53.1 mm
- net Net-(U7-1A): track 0.00 -> 4.69 mm, vias 0 -> 1
- net Net-(U35-1A): track 0.00 -> 4.69 mm, vias 0 -> 1
- net Net-(U31-1A): track 0.00 -> 4.69 mm, vias 0 -> 1
- net Net-(U43-1A): track 0.00 -> 4.69 mm, vias 0 -> 1
- net Net-(U12-1A): track 0.00 -> 4.69 mm, vias 0 -> 1
- net Net-(U39-1A): track 0.00 -> 4.69 mm, vias 0 -> 1
- net Net-(U37-1A): track 0.00 -> 4.69 mm, vias 0 -> 1
- net Net-(U29-1A): track 0.00 -> 4.69 mm, vias 0 -> 1
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- added copper zone on In5.Cu, net VADJ
- removed copper zone on In2.Cu, net VADJ
